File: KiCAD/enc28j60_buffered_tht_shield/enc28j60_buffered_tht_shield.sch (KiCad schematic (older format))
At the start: 8 parts, among them P1 Power, P2 Analog, P3 Digital, P4 Digital, P5 CONN_01X01, P6 CONN_01X01, P7 CONN_01X01, P8 CONN_01X01

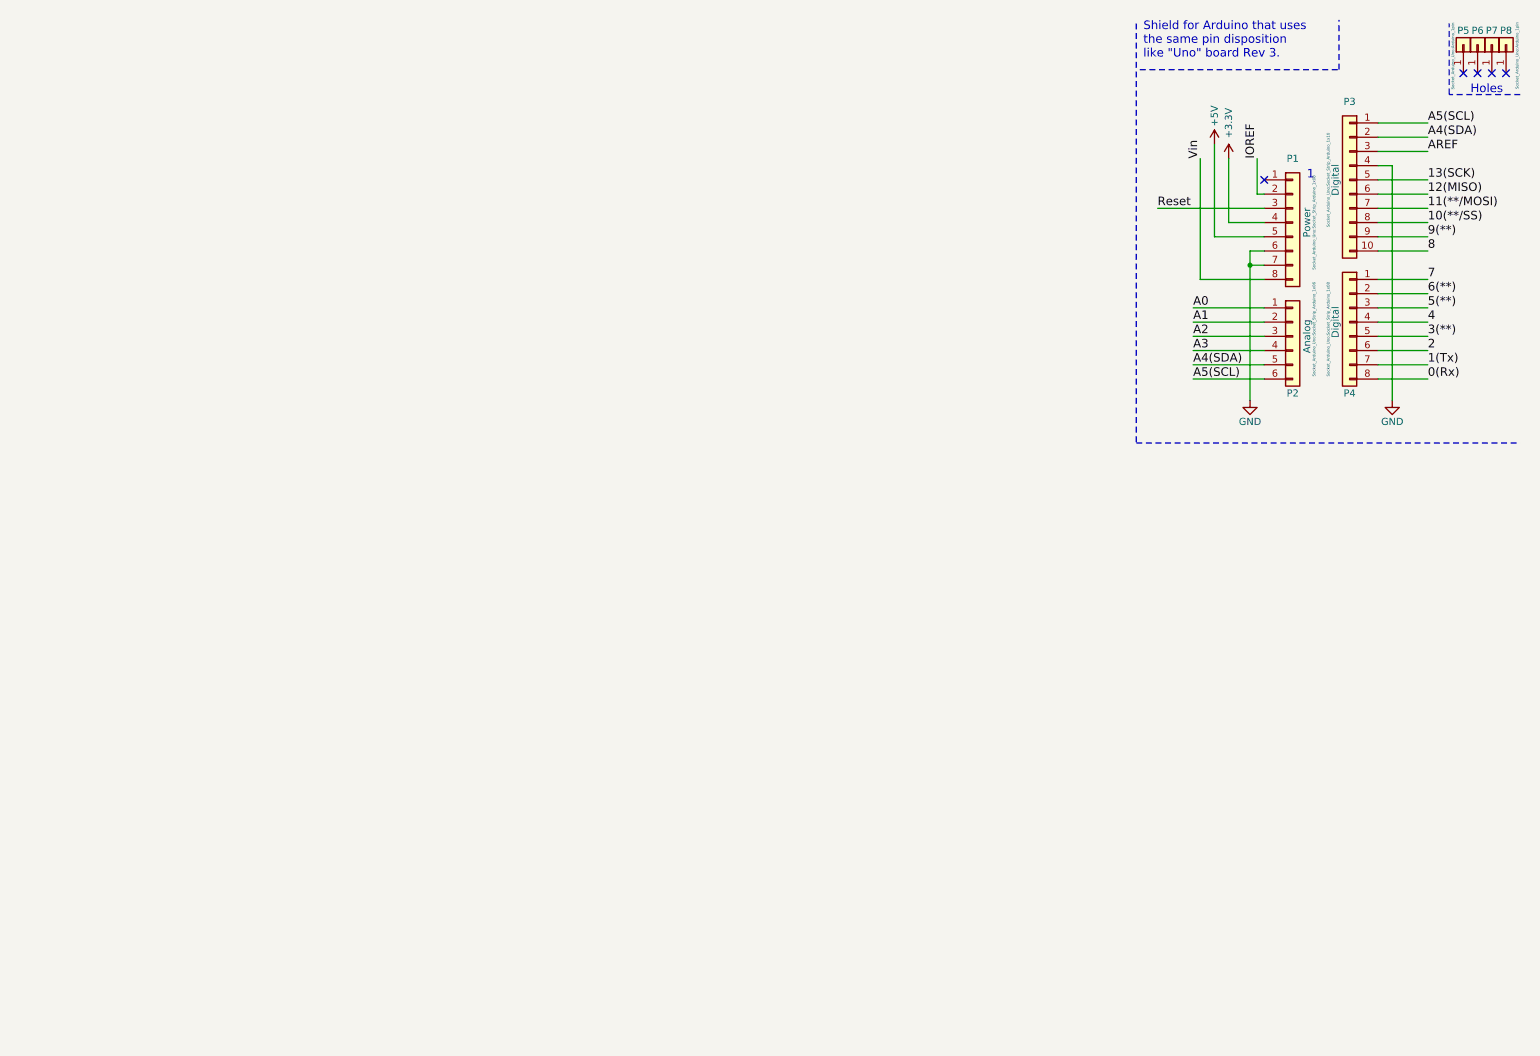
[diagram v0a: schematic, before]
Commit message: Revision 1. 74HCT125N LM1117 3.3 ENC28J60
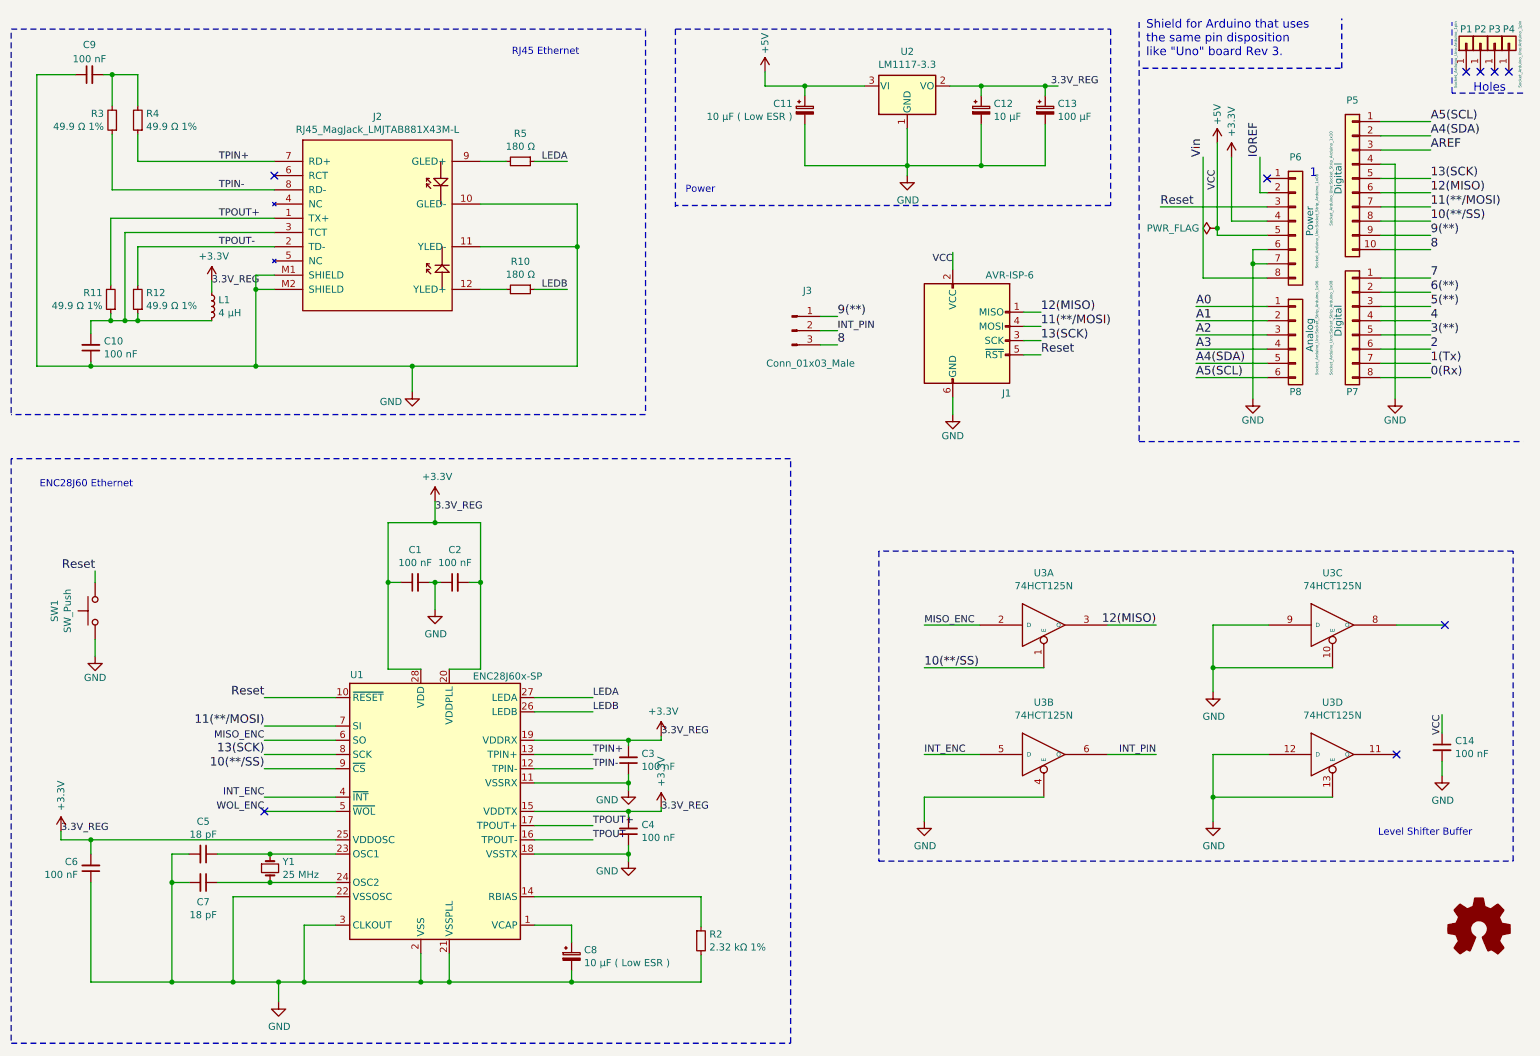
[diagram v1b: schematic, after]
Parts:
- added C1, C10, C14, C2, C3, C4, C6, C9: 100 nF, Capacitor_THT:C_Disc_D4.7mm_W2.5mm_P5.00mm, symbol Device:C_Small
- added C11, C8: 10 μF ( Low ESR ), Capacitor_THT:CP_Radial_Tantal_D4.5mm_P2.50mm, symbol Device:CP_Small
- added C12: 10 μF, Capacitor_THT:CP_Radial_D5.0mm_P2.00mm, symbol Device:CP_Small
- added C13: 100 μF, Capacitor_THT:CP_Radial_D5.0mm_P2.00mm, symbol Device:CP_Small
- added C5, C7: 18 pF, Capacitor_THT:C_Disc_D4.7mm_W2.5mm_P5.00mm, symbol Device:C_Small
- added J1: AVR-ISP-6, Connector_PinSocket_2.54mm:PinSocket_2x03_P2.54mm_Vertical, symbol Connector:AVR-ISP-6
- added J2: RJ45_MagJack_LMJTAB881X43M-L, RJ45_MagJack_LMJTAB881X43M-L:RJ45_MagJack_LMJTAB881X43M-L, symbol RJ45_MagJack_LMJTAB881X43M-L:RJ45_MagJack_LMJTAB881X43M-L
- added J3: Conn_01x03_Male, Connector_PinHeader_2.54mm:PinHeader_1x03_P2.54mm_Vertical, symbol Connector:Conn_01x03_Male
- added L1: 4 μH, Inductor_THT:L_Axial_L6.6mm_D2.7mm_P2.54mm_Vertical_Vishay_IM-2, symbol Device:L_Small
- added R10: 180 Ω, Resistor_THT:R_Axial_DIN0207_L6.3mm_D2.5mm_P5.08mm_Vertical, symbol Device:R_Small
- added R11, R12, R3, R4: 49.9 Ω 1%, Resistor_THT:R_Axial_DIN0207_L6.3mm_D2.5mm_P5.08mm_Vertical, symbol Device:R_Small
- added R2: 2.32 kΩ 1%, Resistor_THT:R_Axial_DIN0207_L6.3mm_D2.5mm_P7.62mm_Horizontal, symbol Device:R_Small
- added R5: 180 Ω, Resistor_THT:R_Axial_DIN0207_L6.3mm_D2.5mm_P7.62mm_Horizontal, symbol Device:R_Small
- added SW1: SW_Push, Button_Switch_THT:SW_PUSH_6mm_H5mm, symbol Switch:SW_Push
- added U1: ENC28J60x-SP, Package_DIP:DIP-28_W7.62mm_Socket_LongPads, symbol Interface_Ethernet:ENC28J60x-SP
- added U2: LM1117-3.3, Package_TO_SOT_THT:TO-220-3_Horizontal_TabDown, symbol Regulator_Linear:LM1117-3.3
- added U3: 74HCT125N, Package_DIP:DIP-14_W7.62mm_Socket_LongPads, symbol 74HCT125N:74HCT125N
- added Y1: 25 MHz, Crystal:Crystal_HC49-4H_Vertical, symbol Device:Crystal_Small
- renumbered P5 to P1, P6 to P2, P7 to P3, P8 to P4, P3 to P5, P1 to P6, P4 to P7, P2 to P8
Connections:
- net labels added: 3.3V_REG, INT_ENC, INT_PIN, LEDA, LEDB, MISO_ENC, TPIN+, TPIN-, TPOUT+, TPOUT-, VCC, WOL_ENC
- wire segments 38 -> 204
- no-connect marks 5 -> 9
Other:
- note added: "ENC28J60 Ethernet"
- note added: "Level Shifter Buffer"
- note added: "Power"
- note added: "RJ45 Ethernet"
- moved on the sheet: P1, P2, P3, P4, P5, P6, P7, P8

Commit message: Fixed AVR-ISP-PINS
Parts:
- J1: footprint Connector_PinSocket_2.54mm:PinSocket_2x03_P2.54mm_Vertical -> Connector_IDC:IDC-Header_2x03_P2.54mm_Vertical
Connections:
- net labels added: CLKOUT_ENC
- wire segments 204 -> 203
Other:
- moved on the sheet: C14
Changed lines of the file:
@@
 Connection ~ 2470 7240
-Wire Wire Line
-	2470 7240 2650 7240
 Wire Wire Line
 	4270 6640 5440 6640
@@
 	4930 6040 4930 6080
 Wire Wire Line
-	4930 6340 4930 6390
-Wire Wire Line
-	4930 6280 4930 6340
-Connection ~ 4930 6340
-Wire Wire Line
 	4930 6040 5160 6040
 Wire Wire Line
@@
 	4930 5840 4930 5780
 Connection ~ 4930 5840
-Wire Wire Line
-	4270 6340 4930 6340
 $Comp
 L Device:C_Small C1
@@
 	5440 6850 5440 6640
 Wire Wire Line
-	2870 6840 2650 6840
-Wire Wire Line
-	2650 6840 2650 7240
-Connection ~ 2650 7240
-Wire Wire Line
-	2650 7240 3470 7240
-Wire Wire Line
 	3240 4430 3240 5040
 Wire Wire Line
@@
 $Comp
 L 74HCT125N:74HCT125N U3
-U 3 1 5C1AC4D0
-P 9880 4730
-F 0 "U3" H 9880 5096 50  0000 C CNN
-F 1 "74HCT125N" H 9880 5005 50  0000 C CNN
-F 2 "Package_DIP:DIP-14_W7.62mm_Socket_LongPads" H 9880 4730 50  0001 C CNN
-F 3 "" H 9880 4730 50  0001 C CNN
-	3    9880 4730
-	1    0    0    -1
-$EndComp
-$Comp
-L 74HCT125N:74HCT125N U3
-U 4 1 5C1AC592
+U 3 1 5C1AC592
 P 9880 5640
 F 0 "U3" H 9880 6006 50  0000 C CNN
@@
 F 2 "Package_DIP:DIP-14_W7.62mm_Socket_LongPads" H 9880 5640 50  0001 C CNN
 F 3 "" H 9880 5640 50  0001 C CNN
-	4    9880 5640
+	3    9880 5640
 	1    0    0    -1
 $EndComp
@@
 Wire Wire Line
 	8300 5640 8640 5640
-$Comp
-L power:GND #PWR0105
-U 1 1 5C1E75AD
-P 7010 6110
-F 0 "#PWR0105" H 7010 5860 50  0001 C CNN
-F 1 "GND" H 7015 5937 50  0000 C CNN
-F 2 "" H 7010 6110 50  0001 C CNN
-F 3 "" H 7010 6110 50  0001 C CNN
-	1    7010 6110
-	1    0    0    -1
-$EndComp
 Wire Wire Line
 	7010 5940 7010 6110
 Wire Wire Line
-	9430 4730 9040 4730
-Wire Wire Line
-	9880 5030 9040 5030
-Wire Wire Line
 	9430 5640 9040 5640
 Wire Wire Line
 	9880 5940 9040 5940
-Wire Wire Line
-	9040 5940 9040 5640
-NoConn ~ 10330 5640
 Wire Wire Line
 	6890 1500 7410 1500
@@
 L Device:C_Small C14
 U 1 1 5C5AE356
-P 10650 5590
-F 0 "C14" H 10742 5636 50  0000 L CNN
-F 1 "100 nF" H 10742 5545 50  0000 L CNN
-F 2 "Capacitor_THT:C_Disc_D4.7mm_W2.5mm_P5.00mm" H 10650 5590 50  0001 C CNN
-F 3 "~" H 10650 5590 50  0001 C CNN
-	1    10650 5590
-	1    0    0    -1
-$EndComp
-$Comp
-L power:GND #PWR021
-U 1 1 5C5AE807
-P 10650 5790
-F 0 "#PWR021" H 10650 5540 50  0001 C CNN
-F 1 "GND" H 10655 5617 50  0000 C CNN
-F 2 "" H 10650 5790 50  0001 C CNN
-F 3 "" H 10650 5790 50  0001 C CNN
-	1    10650 5790
-	1    0    0    -1
-$EndComp
-Wire Wire Line
-	10650 5360 10650 5490
-Wire Wire Line
-	10650 5690 10650 5790
-$Comp
-L power:GND #PWR0106
-U 1 1 5C66D6A7
-P 9040 5200
-F 0 "#PWR0106" H 9040 4950 50  0001 C CNN
-F 1 "GND" H 9045 5027 50  0000 C CNN
-F 2 "" H 9040 5200 50  0001 C CNN
-F 3 "" H 9040 5200 50  0001 C CNN
-	1    9040 5200
-	1    0    0    -1
-$EndComp
+P 10630 5120
+F 0 "C14" H 10722 5166 50  0000 L CNN
+F 1 "100 nF" H 10722 5075 50  0000 L CNN
+F 2 "Capacitor_THT:C_Disc_D4.7mm_W2.5mm_P5.00mm" H 10630 5120 50  0001 C CNN
+F 3 "~" H 10630 5120 50  0001 C CNN
+	1    10630 5120
+	1    0    0    -1
+$EndComp
+Wire Wire Line
+	10630 4890 10630 5020
+Wire Wire Line
+	10630 5220 10630 5320
 Text Notes 5330 1700 0    50   ~ 0
 Power
@@
 Level Shifter Buffer
 Wire Wire Line
-	10330 4730 10670 4730
-Wire Wire Line
-	9040 5030 9040 5200
-$Comp
-L power:GND #PWR0107
-U 1 1 5CA6E031
-P 9040 6110
-F 0 "#PWR0107" H 9040 5860 50  0001 C CNN
-F 1 "GND" H 9045 5937 50  0000 C CNN
-F 2 "" H 9040 6110 50  0001 C CNN
-F 3 "" H 9040 6110 50  0001 C CNN
-	1    9040 6110
-	1    0    0    -1
-$EndComp
-Wire Wire Line
 	9040 5940 9040 6110
-Connection ~ 9040 5940
 Wire Notes Line
 	5260 540  5260 1790
@@
 Wire Wire Line
 	2370 5240 2870 5240
-NoConn ~ 10670 4730
-Wire Wire Line
-	9040 5030 9040 4730
-Connection ~ 9040 5030
 Wire Wire Line
 	7830 2630 7710 2630
@@
 F 0 "J1" H 7620 2360 50  0000 R CNN
 F 1 "AVR-ISP-6" H 7780 3190 50  0000 R CNN
-F 2 "Connector_PinSocket_2.54mm:PinSocket_2x03_P2.54mm_Vertical" V 7060 2780 50  0001 C CNN
+F 2 "Connector_IDC:IDC-Header_2x03_P2.54mm_Vertical" V 7060 2780 50  0001 C CNN
 F 3 " ~" H 6035 2180 50  0001 C CNN
 	1    7310 2730
@@
 Wire Wire Line
 	9070 1940 9070 1340
-Text Label 10650 5360 3    50   ~ 0
+Text Label 10630 4890 3    50   ~ 0
 VCC
 Text Label 7210 2190 2    50   ~ 0
 VCC
+Wire Wire Line
+	2870 6840 2370 6840
+Wire Wire Line
+	2470 7240 3470 7240
+Text Label 2370 6840 0    50   ~ 0
+CLKOUT_ENC
+Wire Wire Line
+	10330 5640 10670 5640
+Wire Wire Line
+	4930 6280 4930 6340
+Wire Wire Line
+	4270 6340 4930 6340
+Connection ~ 4930 6340
+Wire Wire Line
+	4930 6340 4930 6390
+$Comp
+L power:GND #PWR0101
+U 1 1 5F602F83
+P 10630 5320
+F 0 "#PWR0101" H 10630 5070 50  0001 C CNN
+F 1 "GND" H 10630 5170 50  0000 C CNN
+F 2 "" H 10630 5320 50  0000 C CNN
+F 3 "" H 10630 5320 50  0000 C CNN
+	1    10630 5320
+	1    0    0    -1
+$EndComp
+$Comp
+L power:GND #PWR0105
+U 1 1 5F6043C6
+P 7010 6110
+F 0 "#PWR0105" H 7010 5860 50  0001 C CNN
+F 1 "GND" H 7010 5960 50  0000 C CNN
+F 2 "" H 7010 6110 50  0000 C CNN
+F 3 "" H 7010 6110 50  0000 C CNN
+	1    7010 6110
+	1    0    0    -1
+$EndComp
+$Comp
+L power:GND #PWR0107
+U 1 1 5F604CE5
+P 9040 6110
+F 0 "#PWR0107" H 9040 5860 50  0001 C CNN
+F 1 "GND" H 9040 5960 50  0000 C CNN
+F 2 "" H 9040 6110 50  0000 C CNN
+F 3 "" H 9040 6110 50  0000 C CNN
+	1    9040 6110
+	1    0    0    -1
+$EndComp
+$Comp
+L power:GND #PWR0106
+U 1 1 5F603973
+P 9040 5200
+F 0 "#PWR0106" H 9040 4950 50  0001 C CNN
+F 1 "GND" H 9040 5050 50  0000 C CNN
+F 2 "" H 9040 5200 50  0000 C CNN
+F 3 "" H 9040 5200 50  0000 C CNN
+	1    9040 5200
+	1    0    0    -1
+$EndComp
+Wire Wire Line
+	9040 5030 9040 5200
+Wire Wire Line
+	9880 5030 9040 5030
+Connection ~ 9040 5030
+Wire Wire Line
+	9040 5030 9040 4730
+NoConn ~ 10670 4730
+Wire Wire Line
+	10330 4730 10670 4730
+Wire Wire Line
+	9430 4730 9040 4730
+$Comp
+L 74HCT125N:74HCT125N U3
+U 4 1 5C1AC4D0
+P 9880 4730
+F 0 "U3" H 9880 5096 50  0000 C CNN
+F 1 "74HCT125N" H 9880 5005 50  0000 C CNN
+F 2 "Package_DIP:DIP-14_W7.62mm_Socket_LongPads" H 9880 4730 50  0001 C CNN
+F 3 "" H 9880 4730 50  0001 C CNN
+	4    9880 4730
+	1    0    0    -1
+$EndComp
+NoConn ~ 10670 5640
+Wire Wire Line
+	9040 5640 9040 5940
+Connection ~ 9040 5940
 $EndSCHEMATC

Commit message: v1
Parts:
- J1: footprint Connector_IDC:IDC-Header_2x03_P2.54mm_Vertical -> Connector_PinSocket_2.54mm:PinSocket_2x03_P2.54mm_Vertical
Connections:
- net labels removed: CLKOUT_ENC
- no-connect marks 9 -> 10
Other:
- note added: "ENC Interrupt Selection ( 8 or 9 )"
- moved on the sheet: C1, C10, C11, C12, C13, C14, C2, C3, C4, C5, C6, C7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

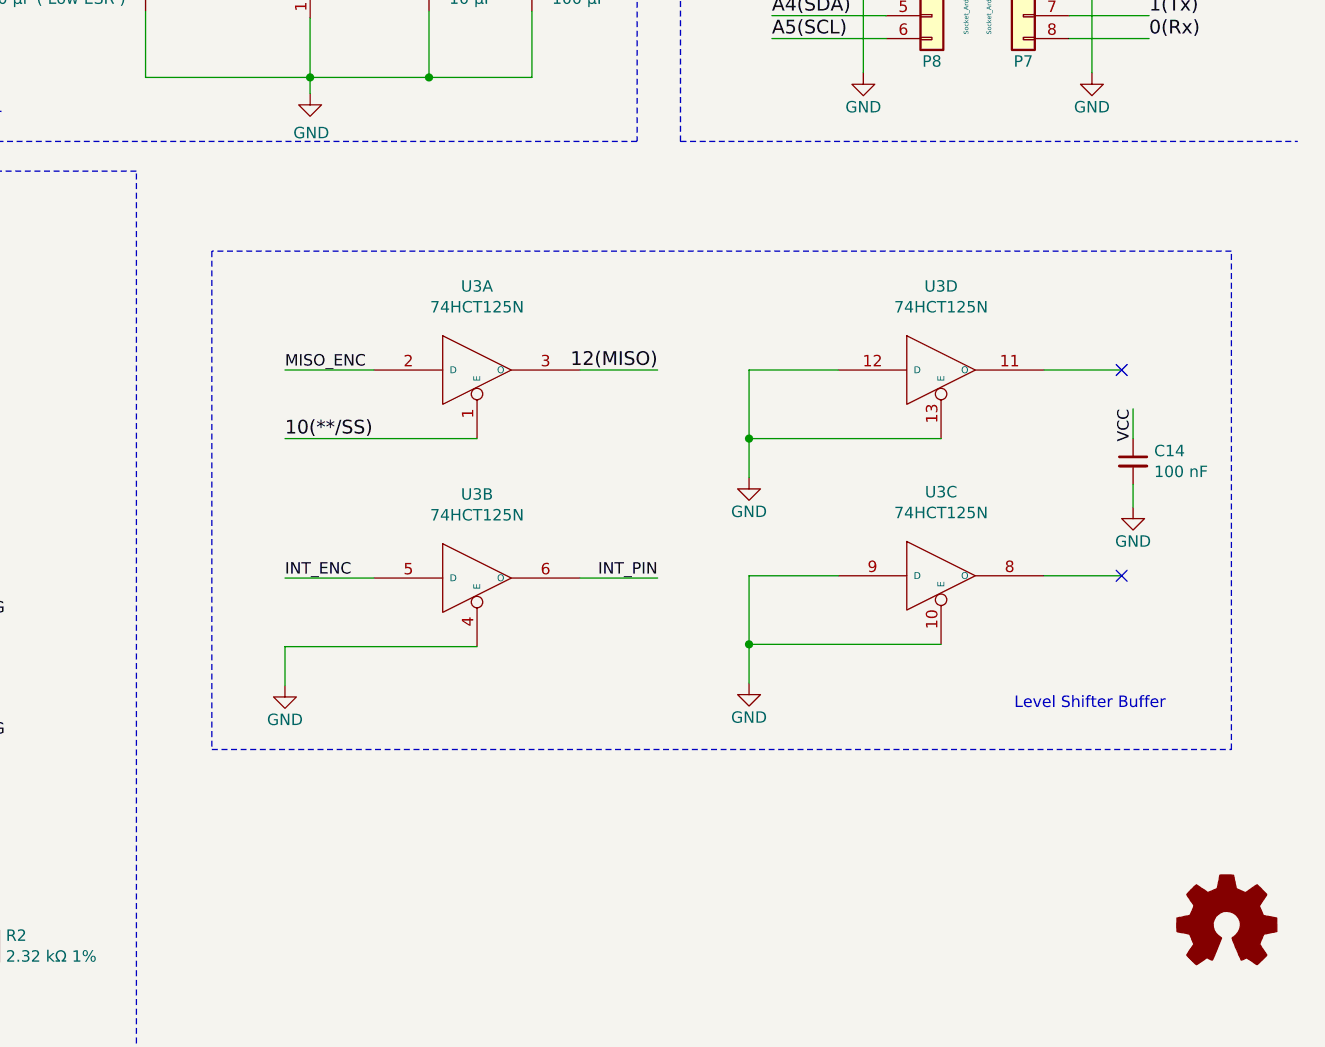
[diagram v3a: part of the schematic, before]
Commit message: Added AT24MAC402-602 as an option.
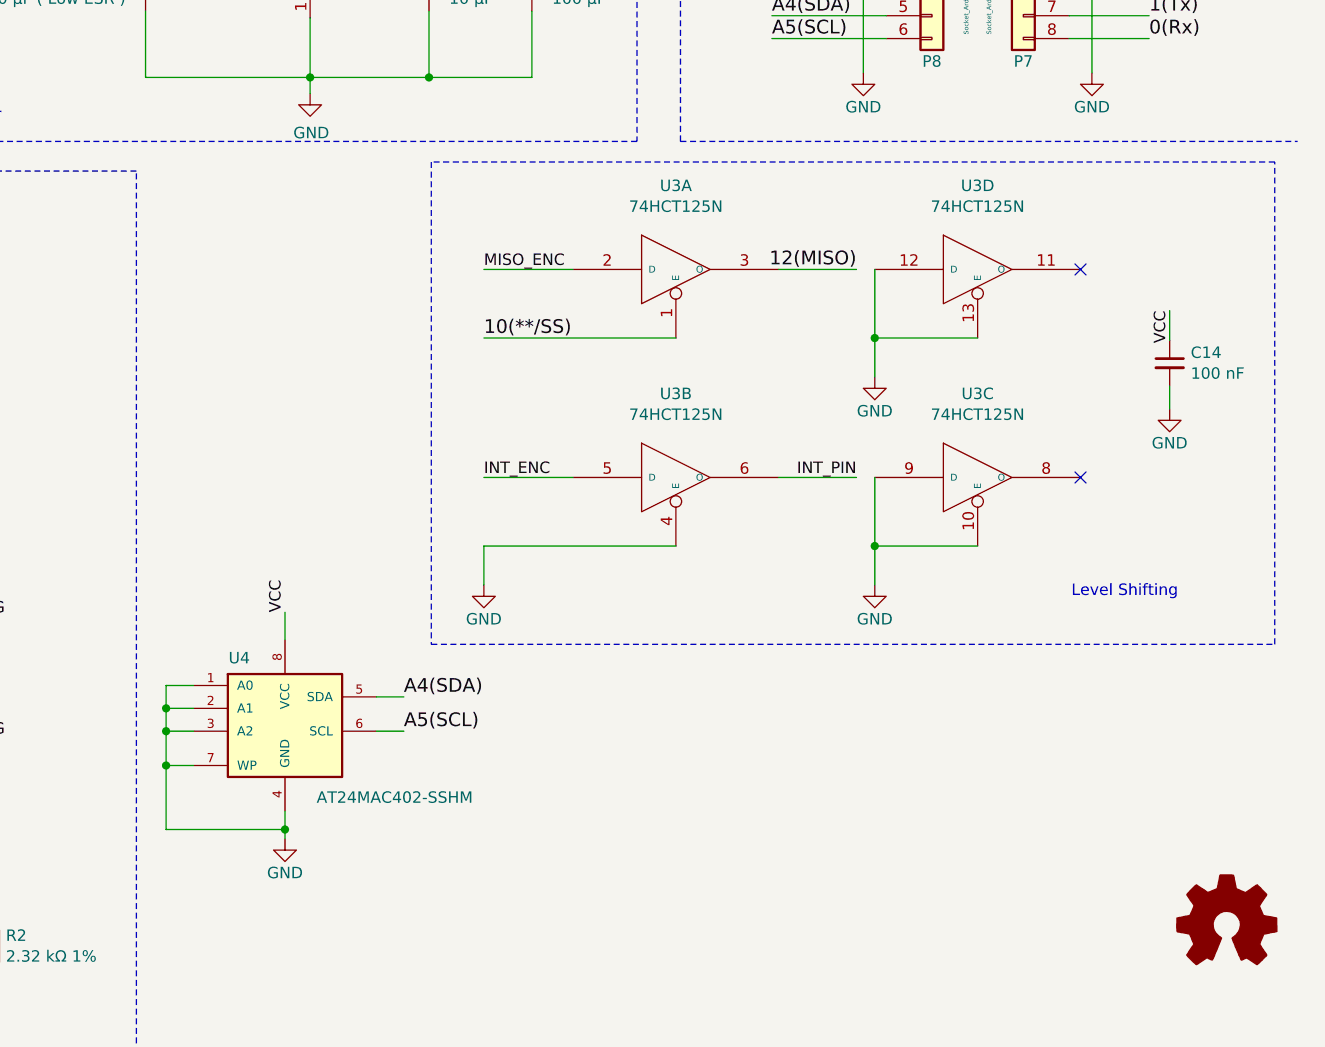
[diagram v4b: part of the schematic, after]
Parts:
- added U4: AT24MAC402-SSHM, Package_DIP:DIP-8_W7.62mm_Socket_LongPads, symbol AT24MAC402-SSHM:AT24MAC402-SSHM
- R2, R5: footprint Resistor_THT:R_Axial_DIN0207_L6.3mm_D2.5mm_P7.62mm_Horizontal -> Resistor_THT:R_Axial_DIN0207_L6.3mm_D2.5mm_P5.08mm_Vertical
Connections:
- wire segments 203 -> 213
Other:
- note added: "Level Shifting"
- note removed: "Level Shifter Buffer"
- moved on the sheet: C14, U3A, U3B, U3C, U3D
